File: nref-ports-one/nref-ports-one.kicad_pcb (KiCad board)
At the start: 4 copper layers, 88 x 35.5 mm, 118 parts, among them J1 CONN_HEAD, J10 CONN_SPK, J2 DM3AT-SF-PEJM5, J3 09452812561, J4 USB_C_Receptacle, J5 Conn_01x10_Pin, J6 Conn_01x14_Pin, J7 Conn_01x12_Pin, J8 PWR, J9 Conn_01x10_Pin, U1 TPS7A0533PDBZ, U10 HD3SS3220IRNHT, U11 PCAL6416AHF, U12 TLV75518PDBV, U2 TLV320AIC3100, U3 TXS0108EPW, U4 SN74AVC1T45, U5 TPD4E02B04DQA, U6 TPD4E02B04DQA, U7 TPD4E02B04DQA, U8 FUSB302BMPX, U9 AP22815A

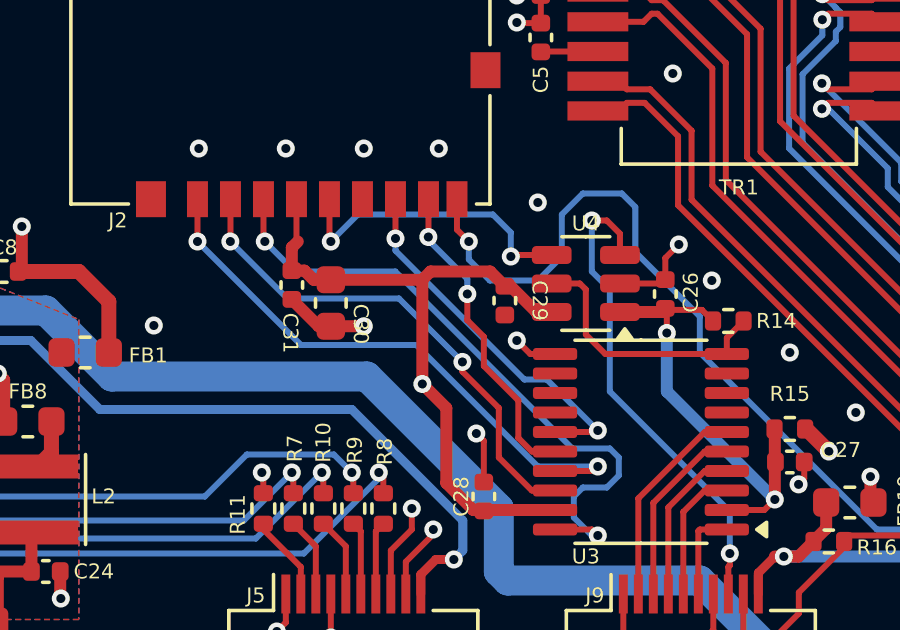
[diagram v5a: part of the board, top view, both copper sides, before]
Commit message: batterypack and ports one snapshot
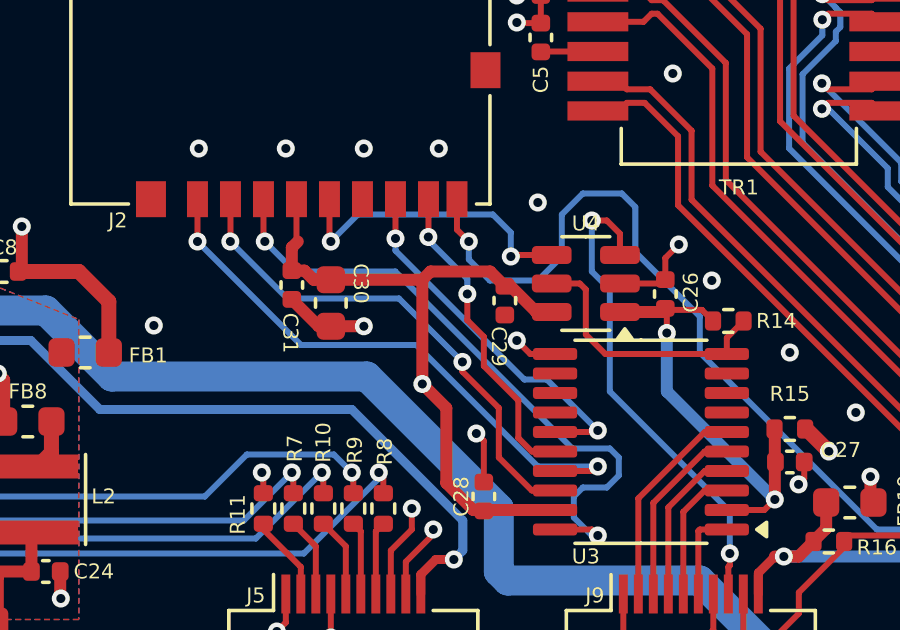
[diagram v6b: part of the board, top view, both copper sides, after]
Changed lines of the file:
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@@
 			)
 		)
+		(model "${KIPRJMOD}/3d-models/HX5084NLT.stp"
+			(offset
+				(xyz 0 0 2)
+			)
+			(scale
+				(xyz 1 1 1)
+			)
+			(rotate
+				(xyz 0 0 90)
+			)
+		)
 	)
 	(footprint "Resistor_SMD:R_0402_1005Metric"
@@
 		(tags "capacitor")
 		(property "Reference" "C30"
-			(at 0.7 -1 -90)
+			(at -0.65 -1 -90)
 			(unlocked yes)
 			(layer "F.SilkS")
@@
 		)
 		(property "Value" "0"
-			(at 0 1.17 360)
+			(at 0 1.17 0)
 			(layer "F.Fab")
 			(effects
@@
 		)
 		(fp_text user "${REFERENCE}"
-			(at 0 0 360)
+			(at 0 0 0)
 			(layer "F.Fab")
 			(effects
@@
 		(tags "capacitor")
 		(property "Reference" "C29"
-			(at 0 -1.16 -90)
+			(at 1.53 0.2 -90)
 			(unlocked yes)
 			(layer "F.SilkS")

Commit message: ports-one: WIP construction site
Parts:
- removed U10: HD3SS3220IRNHT, footprints:QFN40P450X250X80-31N120X320
- removed U11: PCAL6416AHF, Package_DFN_QFN:HVQFN-24-1EP_4x4mm_P0.5mm_EP2.1x2.1mm
- moved J10 66.2 mm to (184.8, 126.2), turned to 90 degrees
- moved J7 48.0 mm to (119.9, 133.0)
- moved C37 7.83 mm to (181.8, 119.8)
- moved U8 5.93 mm to (184.2, 118.9)
- moved FB1 2.66 mm to (121.7, 120.6), turned to -90 degrees
- moved C23 1.38 mm to (116.9, 129.1)
- moved C24 1.35 mm to (121.3, 129.1)
- moved C25 1.35 mm to (119.1, 129.1)
- moved L1 1.27 mm to (117.3, 126.8)
- moved L2 1.26 mm to (121.0, 126.8)
- moved FB8 1.22 mm to (120.6, 124.2)
- moved FB9 1.22 mm to (117.6, 124.2)
- moved C18 1.07 mm to (115.1, 123.9)
- moved R13 1.05 mm to (115.1, 123.0)
- moved C22 0.55 mm to (117.0, 123.0)
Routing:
- net Net-(U10-CC2): track 66.3 -> 0.46 mm, vias 3 -> 1
- net USB_VBUS: track 94.6 -> 38.0 mm, vias 10 -> 7
- net RP_SCL0: track 49.0 -> 3.30 mm, vias 3 -> 2
- net RP_FUSB_INT: track 46.3 -> 1.43 mm, vias 2 -> 1
- net STANDBY_3V3: track 53.0 -> 8.31 mm
- net Net-(U10-CC1): track 65.8 -> 23.4 mm, vias 3 -> 1
- net RP_SDA0: track 44.8 -> 4.53 mm
- net USB1_DP: track 32.2 -> 0.00 mm, vias 4 -> 0
- net USB1_DN: track 29.2 -> 0.00 mm, vias 2 -> 0
- net GND: track 119.0 -> 89.8 mm, vias 75 -> 66
- net USB_SRC_EN: track 32.5 -> 7.79 mm, vias 4 -> 2
- net CC2: track 22.6 -> 1.00 mm, vias 3 -> 0
- net USBH_2A_RXN: track 20.0 -> 0.00 mm, vias 4 -> 0
- net USBH_2A_RXP: track 18.4 -> 0.00 mm, vias 4 -> 0
- net USB1_TXN: track 18.1 -> 0.00 mm, vias 2 -> 0
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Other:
- board text added: "Stackup: JLC04161H-3313 90 ohms coplanar diff pairs, w: 0.1547mm, s: 0.2mm"
